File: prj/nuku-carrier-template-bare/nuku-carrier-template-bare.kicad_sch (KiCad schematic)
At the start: 0 parts

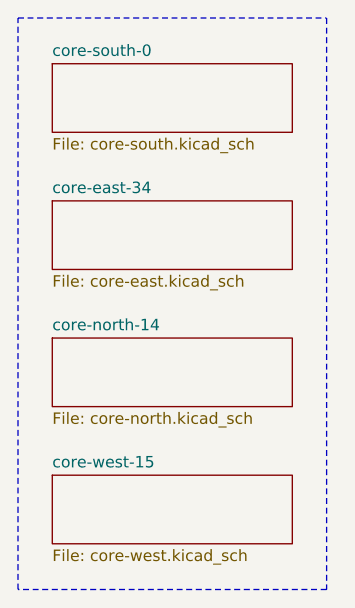
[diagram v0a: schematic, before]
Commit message: Update nuku.carrier.template to template.bare
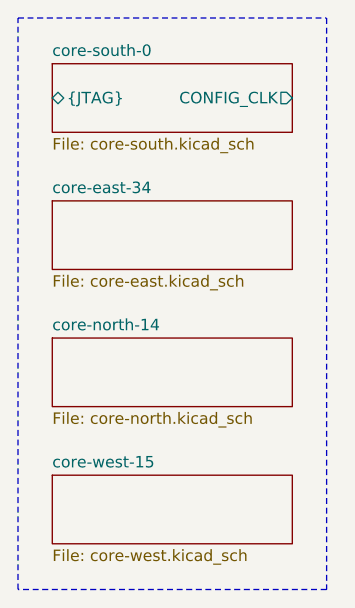
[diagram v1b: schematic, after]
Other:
- sheet core-south-0 ports: added CONFIG_CLK, {JTAG}; removed none
- company: (none) -> Samuel López Asunción
- title: (none) -> nuku.carrier.template.bare
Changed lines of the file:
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@@
 	(generator_version "9.0")
 	(paper "A4")
+	(title_block
+		(title "nuku.carrier.template.bare")
+		(date "2025-06-09")
+		(rev "0")
+		(company "Samuel López Asunción")
+		(comment 1 "@supersmau")
+	)
 	(bus_alias "CONFIG"
 		(members "CONFIG_CLK" "CONFIG_M0" "CONFIG_M1" "CONFIG_M2" "CONFIG_DONE"
@@
 		)
 		(instances
-			(project "nuku-carrier-template"
+			(project "nuku-carrier-template-bare"
 				(path "/15e0a42f-48e0-4a5d-9b6b-7d249ffc02ad"
 					(page "4")
@@
 		)
 		(instances
-			(project "nuku-carrier-template"
+			(project "nuku-carrier-template-bare"
 				(path "/15e0a42f-48e0-4a5d-9b6b-7d249ffc02ad"
 					(page "3")
@@
 			)
 		)
-		(instances
-			(project "nuku-carrier-template"
+		(pin "CONFIG_CLK" output
+			(at 157.48 72.39 0)
+			(effects
+				(font
+					(size 1.27 1.27)
+				)
+				(justify right)
+			)
+		)
+		(pin "{JTAG}" bidirectional
+			(at 130.81 72.39 180)
+			(effects
+				(font
+					(size 1.27 1.27)
+				)
+				(justify left)
+			)
+		)
+		(instances
+			(project "nuku-carrier-template-bare"
 				(path "/15e0a42f-48e0-4a5d-9b6b-7d249ffc02ad"
 					(page "2")
@@
 		)
 		(instances
-			(project "nuku-carrier-template"
+			(project "nuku-carrier-template-bare"
 				(path "/15e0a42f-48e0-4a5d-9b6b-7d249ffc02ad"
 					(page "5")

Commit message: Route template.basic
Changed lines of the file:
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@@
 		(comment 1 "@supersmau")
-	)
-	(bus_alias "CONFIG"
-		(members "CONFIG_CLK" "CONFIG_M0" "CONFIG_M1" "CONFIG_M2" "CONFIG_DONE"
-			"CONFIG_INIT" "CONFIG_PROG" "CONFIG_CFGBVS"
-		)
 	)
 	(bus_alias "JTAG"
@@
 		)
 		(pin "CONFIG_CLK" output
-			(at 157.48 72.39 0)
+			(at 157.48 71.12 0)
 			(effects
 				(font
@@
 		)
 		(pin "{JTAG}" bidirectional
-			(at 130.81 72.39 180)
+			(at 130.81 71.12 180)
 			(effects
 				(font
